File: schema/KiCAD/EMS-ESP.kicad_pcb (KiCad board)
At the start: 2 copper layers, 76.5 x 47.2 mm, 47 parts, among them IC1 LM393N, J1 EMS-Bus, J2 DS18B20, J3 I2C, J4 I2C-BMP180, T1 BC847B, U1 DC-Buck_Converter_Chin01, U2 NodeMCU_1.0_(ESP-12E)

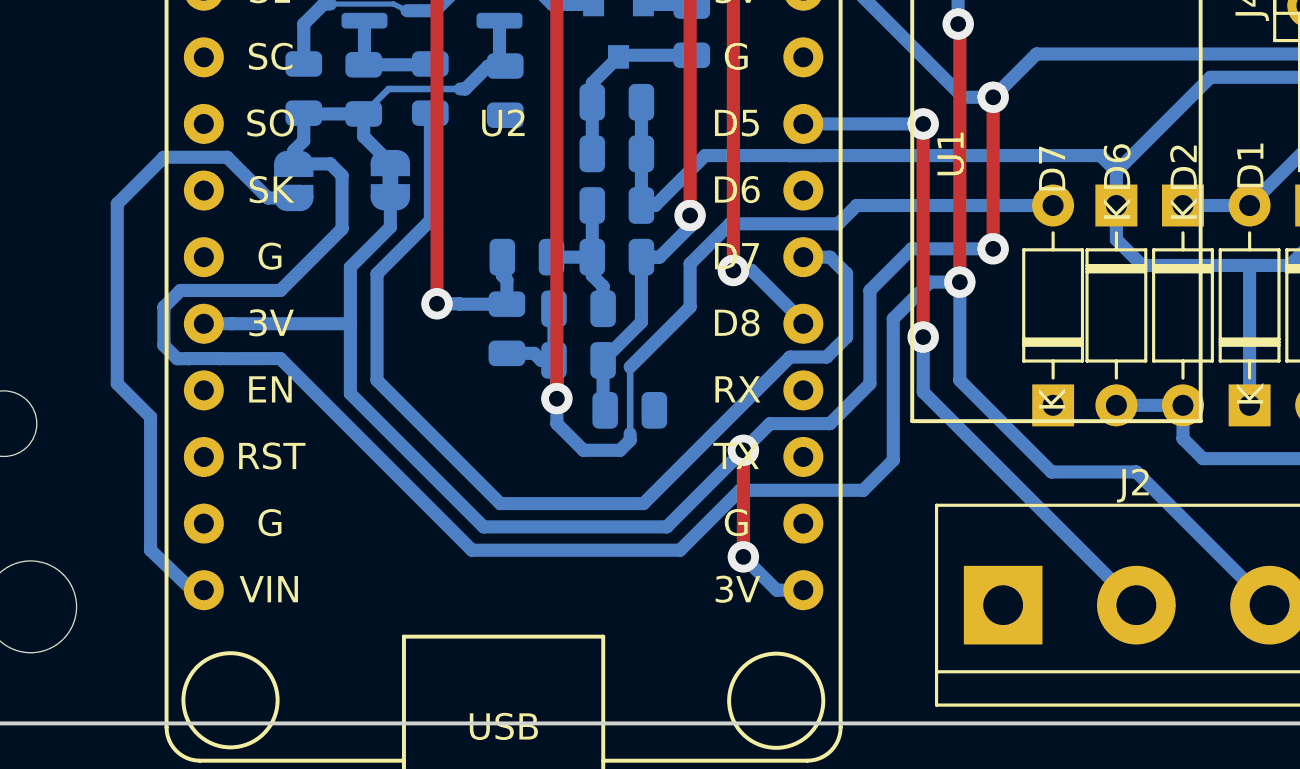
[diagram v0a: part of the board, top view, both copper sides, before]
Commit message: added pullup resistor for DS18B20 data line
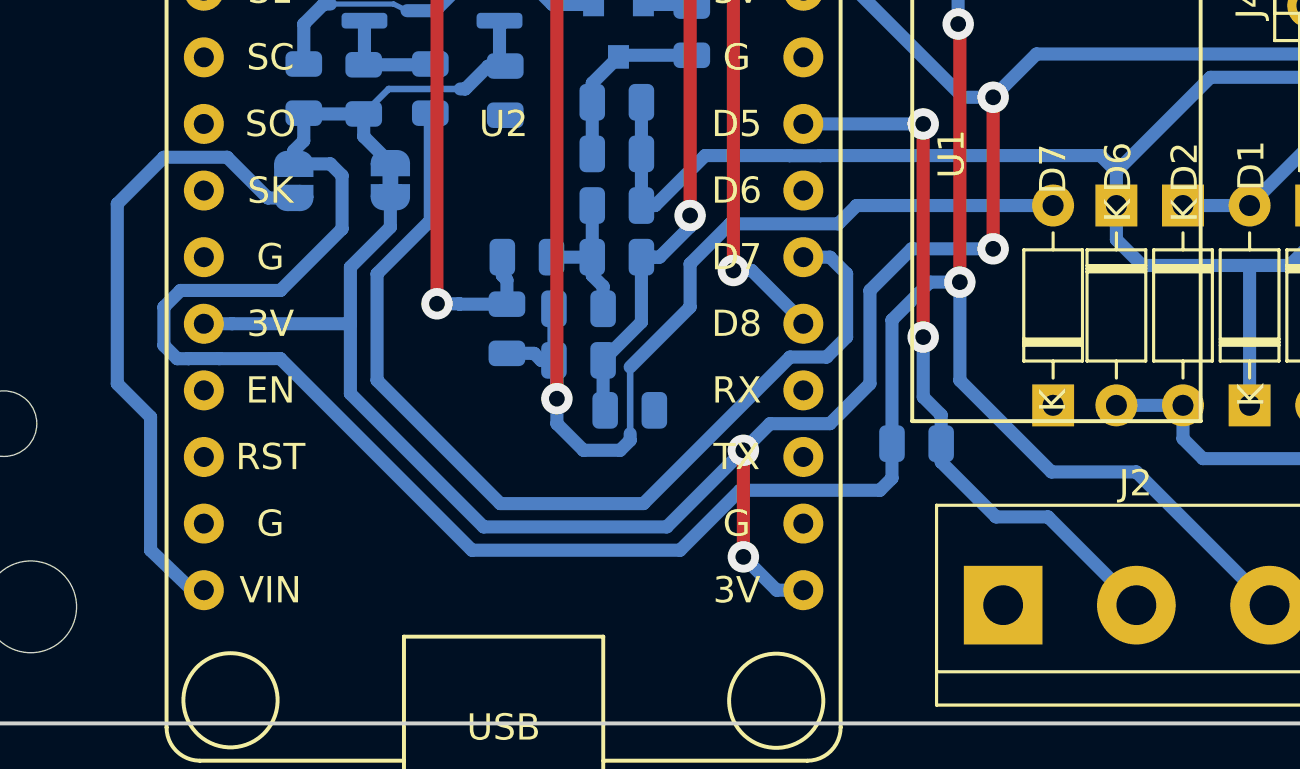
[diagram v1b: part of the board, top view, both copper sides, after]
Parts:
- added R12: 4k7, Resistor_SMD:R_0805_2012Metric, B.Cu at (168.4, 112.0)
- R3: value 360R -> 360
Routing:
- net /DS: track 26.2 -> 27.4 mm
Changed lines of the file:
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@@
     (thickness 1.6)
     (drawings 9)
-    (tracks 292)
+    (tracks 297)
     (zones 0)
-    (modules 47)
+    (modules 48)
     (nets 42)
   )
   (page A4)
   (layers
-    (0 F.Cu signal hide)
+    (0 F.Cu signal)
     (31 B.Cu signal)
     (32 B.Adhes user hide)
@@
     (visible_elements 7FFFFFFF)
     (pcbplotparams
-      (layerselection 0x00020_7ffffffe)
+      (layerselection 0x00010_7ffffffe)
       (usegerberextensions false)
       (usegerberattributes false)
@@
       (subtractmaskfromsilk false)
       (outputformat 4)
-      (mirror false)
+      (mirror true)
       (drillshape 1)
       (scaleselection 1)
@@
       (effects (font (size 1 1) (thickness 0.15)) (justify mirror))
     )
-    (fp_text value 360R (at 0 -1.65) (layer B.Fab)
+    (fp_text value 360 (at 0 -1.65) (layer B.Fab)
       (effects (font (size 1 1) (thickness 0.15)) (justify mirror))
     )
@@
       (net 41 "Net-(U2-Pad30)"))
   )
+  (module Resistor_SMD:R_0805_2012Metric (layer B.Cu)
+    (at 168.402 112.014)
+    (descr "Resistor SMD 0805 (2012 Metric), square (rectangular) end terminal, IPC_7351 nominal, (Body size source: https://docs.google.com/spreadsheets/d/1BsfQQcO9C6DZCsRaXUlFlo91Tg2WpOkGARC1WS5S8t0/edit?usp=sharing), generated with kicad-footprint-generator")
+    (tags resistor)
+    (attr smd)
+    (fp_text reference R12 (at 0 1.65) (layer B.SilkS)
+      (effects (font (size 1 1) (thickness 0.15)) (justify mirror))
+    )
+    (fp_text value 4k7 (at 0 -1.65) (layer B.Fab)
+      (effects (font (size 1 1) (thickness 0.15)) (justify mirror))
+    )
+    (fp_line (start -1 -0.6) (end -1 0.6) (layer B.Fab) (width 0.1))
+    (fp_line (start -1 0.6) (end 1 0.6) (layer B.Fab) (width 0.1))
+    (fp_line (start 1 0.6) (end 1 -0.6) (layer B.Fab) (width 0.1))
+    (fp_line (start 1 -0.6) (end -1 -0.6) (layer B.Fab) (width 0.1))
+    (fp_line (start -0.258578 0.71) (end 0.258578 0.71) (layer B.SilkS) (width 0.12))
+    (fp_line (start -0.258578 -0.71) (end 0.258578 -0.71) (layer B.SilkS) (width 0.12))
+    (fp_line (start -1.68 -0.95) (end -1.68 0.95) (layer B.CrtYd) (width 0.05))
+    (fp_line (start -1.68 0.95) (end 1.68 0.95) (layer B.CrtYd) (width 0.05))
+    (fp_line (start 1.68 0.95) (end 1.68 -0.95) (layer B.CrtYd) (width 0.05))
+    (fp_line (start 1.68 -0.95) (end -1.68 -0.95) (layer B.CrtYd) (width 0.05))
+    (fp_text user %R (at 0 0) (layer B.Fab)
+      (effects (font (size 0.5 0.5) (thickness 0.08)) (justify mirror))
+    )
+    (pad 1 smd roundrect (at -0.9375 0) (size 0.975 1.4) (layers B.Cu B.Paste B.Mask) (roundrect_rratio 0.25)
+      (net 14 +3V3))
+    (pad 2 smd roundrect (at 0.9375 0) (size 0.975 1.4) (layers B.Cu B.Paste B.Mask) (roundrect_rratio 0.25)
+      (net 19 /DS))
+    (model ${KISYS3DMOD}/Resistor_SMD.3dshapes/R_0805_2012Metric.wrl
+      (at (xyz 0 0 0))
+      (scale (xyz 1 1 1))
+      (rotate (xyz 0 0 0))
+    )
+  )
   (gr_line (start 206.502 75.438) (end 206.502 122.682) (layer Edge.Cuts) (width 0.15))
   (gr_line (start 130.048 75.438) (end 206.502 75.438) (layer Edge.Cuts) (width 0.15))
@@
   (segment (start 148.2725 98.4885) (end 147.32 99.441) (width 0.25) (layer B.Cu) (net 14) (status 20))
   (segment (start 151.1935 98.4885) (end 148.2725 98.4885) (width 0.25) (layer B.Cu) (net 14))
-  (segment (start 166.37 113.792) (end 167.513 112.649) (width 0.5) (layer B.Cu) (net 14))
-  (segment (start 161.671 113.792) (end 166.37 113.792) (width 0.5) (layer B.Cu) (net 14))
-  (segment (start 159.385 116.078) (end 161.671 113.792) (width 0.5) (layer B.Cu) (net 14))
-  (segment (start 141.805761 108.769999) (end 141.808691 108.772929) (width 0.5) (layer B.Cu) (net 14))
-  (segment (start 167.513 112.649) (end 167.513 107.2515) (width 0.5) (layer B.Cu) (net 14))
-  (segment (start 146.4945 103.8225) (end 144.145 106.172) (width 0.5) (layer B.Cu) (net 14))
-  (segment (start 168.91 105.8545) (end 170.052996 105.8545) (width 0.5) (layer B.Cu) (net 14))
-  (segment (start 144.653 101.346) (end 146.05 101.346) (width 0.5) (layer B.Cu) (net 14) (status 10))
-  (segment (start 144.145 106.172) (end 140.335 106.172) (width 0.5) (layer B.Cu) (net 14))
-  (segment (start 141.808691 108.772929) (end 144.139499 108.769999) (width 0.5) (layer B.Cu) (net 14))
-  (segment (start 139.7 106.807) (end 139.7 108.2675) (width 0.5) (layer B.Cu) (net 14))
-  (segment (start 146.4945 101.7905) (end 146.4945 103.8225) (width 0.5) (layer B.Cu) (net 14))
-  (segment (start 151.4475 116.078) (end 159.385 116.078) (width 0.5) (layer B.Cu) (net 14))
-  (segment (start 146.05 101.346) (end 146.4945 101.7905) (width 0.5) (layer B.Cu) (net 14))
-  (segment (start 167.513 107.2515) (end 168.91 105.8545) (width 0.5) (layer B.Cu) (net 14))
-  (segment (start 140.636738 108.7755) (end 140.642239 108.769999) (width 0.5) (layer B.Cu) (net 14))
-  (segment (start 144.139499 108.769999) (end 151.4475 116.078) (width 0.5) (layer B.Cu) (net 14))
-  (segment (start 140.335 106.172) (end 139.7 106.807) (width 0.5) (layer B.Cu) (net 14))
-  (segment (start 139.7 108.2675) (end 140.208 108.7755) (width 0.5) (layer B.Cu) (net 14))
-  (segment (start 140.208 108.7755) (end 140.636738 108.7755) (width 0.5) (layer B.Cu) (net 14))
-  (segment (start 140.642239 108.769999) (end 141.805761 108.769999) (width 0.5) (layer B.Cu) (net 14))
   (segment (start 147.32 100.3) (end 148.336 101.316) (width 0.5) (layer B.Cu) (net 14) (status 20))
   (segment (start 147.32 99.441) (end 147.32 100.3) (width 0.5) (layer B.Cu) (net 14) (status 10))
+  (segment (start 167.4645 107.3) (end 167.4645 112.014) (width 0.5) (layer B.Cu) (net 14))
+  (segment (start 170.052996 105.8545) (end 168.91 105.8545) (width 0.5) (layer B.Cu) (net 14))
+  (segment (start 168.91 105.8545) (end 167.4645 107.3) (width 0.5) (layer B.Cu) (net 14))
+  (segment (start 146.4945 101.7905) (end 146.05 101.346) (width 0.5) (layer B.Cu) (net 14))
+  (segment (start 146.4945 103.8225) (end 146.4945 101.7905) (width 0.5) (layer B.Cu) (net 14))
+  (segment (start 144.145 106.172) (end 146.4945 103.8225) (width 0.5) (layer B.Cu) (net 14))
+  (segment (start 139.7 106.807) (end 140.335 106.172) (width 0.5) (layer B.Cu) (net 14))
+  (segment (start 139.7 108.2675) (end 139.7 106.807) (width 0.5) (layer B.Cu) (net 14))
+  (segment (start 140.208 108.7755) (end 139.7 108.2675) (width 0.5) (layer B.Cu) (net 14))
+  (segment (start 161.671 113.792) (end 159.385 116.078) (width 0.5) (layer B.Cu) (net 14))
+  (segment (start 140.636738 108.7755) (end 140.208 108.7755) (width 0.5) (layer B.Cu) (net 14))
+  (segment (start 167.005 113.792) (end 161.671 113.792) (width 0.5) (layer B.Cu) (net 14))
+  (segment (start 146.05 101.346) (end 144.653 101.346) (width 0.5) (layer B.Cu) (net 14))
+  (segment (start 159.385 116.078) (end 151.4475 116.078) (width 0.5) (layer B.Cu) (net 14))
+  (segment (start 140.335 106.172) (end 144.145 106.172) (width 0.5) (layer B.Cu) (net 14))
+  (segment (start 167.4645 112.014) (end 167.4645 113.3325) (width 0.5) (layer B.Cu) (net 14))
+  (segment (start 144.139499 108.769999) (end 141.808691 108.772929) (width 0.5) (layer B.Cu) (net 14))
+  (segment (start 167.4645 113.3325) (end 167.005 113.792) (width 0.5) (layer B.Cu) (net 14))
+  (segment (start 151.4475 116.078) (end 144.139499 108.769999) (width 0.5) (layer B.Cu) (net 14))
+  (segment (start 141.808691 108.772929) (end 141.805761 108.769999) (width 0.5) (layer B.Cu) (net 14))
+  (segment (start 141.805761 108.769999) (end 140.642239 108.769999) (width 0.5) (layer B.Cu) (net 14))
+  (segment (start 140.642239 108.769999) (end 140.636738 108.7755) (width 0.5) (layer B.Cu) (net 14))
   (segment (start 181.102 110.5535) (end 181.102 105.2195) (width 0.5) (layer B.Cu) (net 15) (status 10))
   (segment (start 183.642 104.2035) (end 183.642 102.9335) (width 0.5) (layer B.Cu) (net 15) (status 20))
@@
   (segment (start 193.167 110.5535) (end 193.167 112.7125) (width 0.5) (layer B.Cu) (net 18) (status 10))
   (segment (start 193.167 112.7125) (end 192.532 113.3475) (width 0.5) (layer B.Cu) (net 18))
-  (segment (start 168.655998 108.374264) (end 168.655998 107.95) (width 0.5) (layer B.Cu) (net 19))
-  (segment (start 176.784 118.1735) (end 168.655998 110.045498) (width 0.5) (layer B.Cu) (net 19) (status 10))
   (via (at 168.655998 107.95) (size 1.2) (drill 0.6) (layers F.Cu B.Cu) (net 19))
-  (segment (start 168.655998 110.045498) (end 168.655998 108.374264) (width 0.5) (layer B.Cu) (net 19))
   (segment (start 168.655998 99.822002) (end 168.656 99.822) (width 0.5) (layer F.Cu) (net 19))
   (segment (start 168.655998 107.95) (end 168.655998 99.822002) (width 0.5) (layer F.Cu) (net 19))
   (segment (start 164.1475 99.822) (end 168.656 99.822) (width 0.5) (layer B.Cu) (net 19) (status 10))
   (via (at 168.656 99.822) (size 1.2) (drill 0.6) (layers F.Cu B.Cu) (net 19))
+  (segment (start 169.3395 110.9195) (end 169.3395 112.014) (width 0.5) (layer B.Cu) (net 19))
+  (segment (start 168.655998 107.95) (end 168.655998 110.235998) (width 0.5) (layer B.Cu) (net 19))
+  (segment (start 168.655998 110.235998) (end 169.3395 110.9195) (width 0.5) (layer B.Cu) (net 19))
+  (segment (start 169.3395 112.714) (end 171.4335 114.808) (width 0.5) (layer B.Cu) (net 19))
+  (segment (start 169.3395 112.014) (end 169.3395 112.714) (width 0.5) (layer B.Cu) (net 19))
+  (segment (start 173.4185 114.808) (end 176.784 118.1735) (width 0.5) (layer B.Cu) (net 19))
+  (segment (start 171.4335 114.808) (end 173.4185 114.808) (width 0.5) (layer B.Cu) (net 19))
   (segment (start 183.388 91.5035) (end 183.388 95.3135) (width 0.5) (layer B.Cu) (net 20) (status 30))
   (segment (start 181.4195 89.535) (end 183.388 91.5035) (width 0.5) (layer B.Cu) (net 20) (status 20))

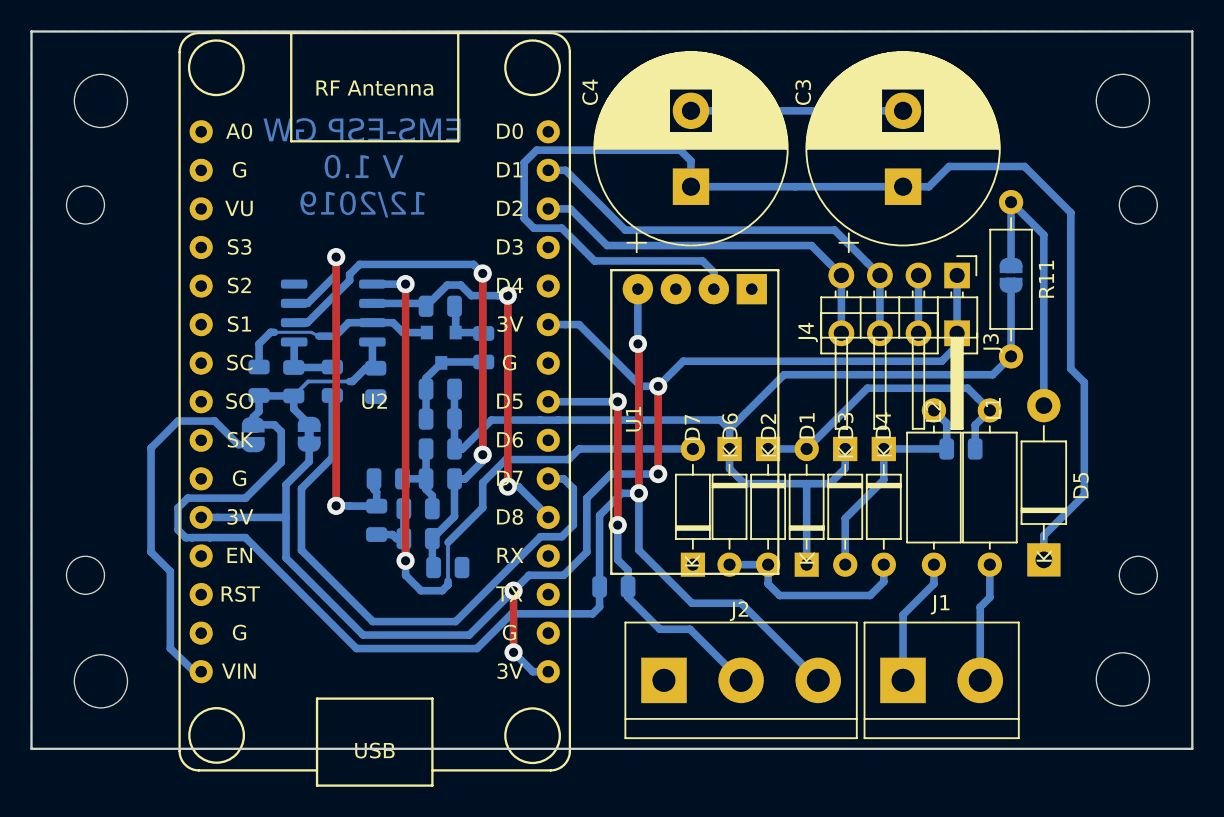
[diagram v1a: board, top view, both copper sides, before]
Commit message: rearranged bucket converter, pinheader corrected
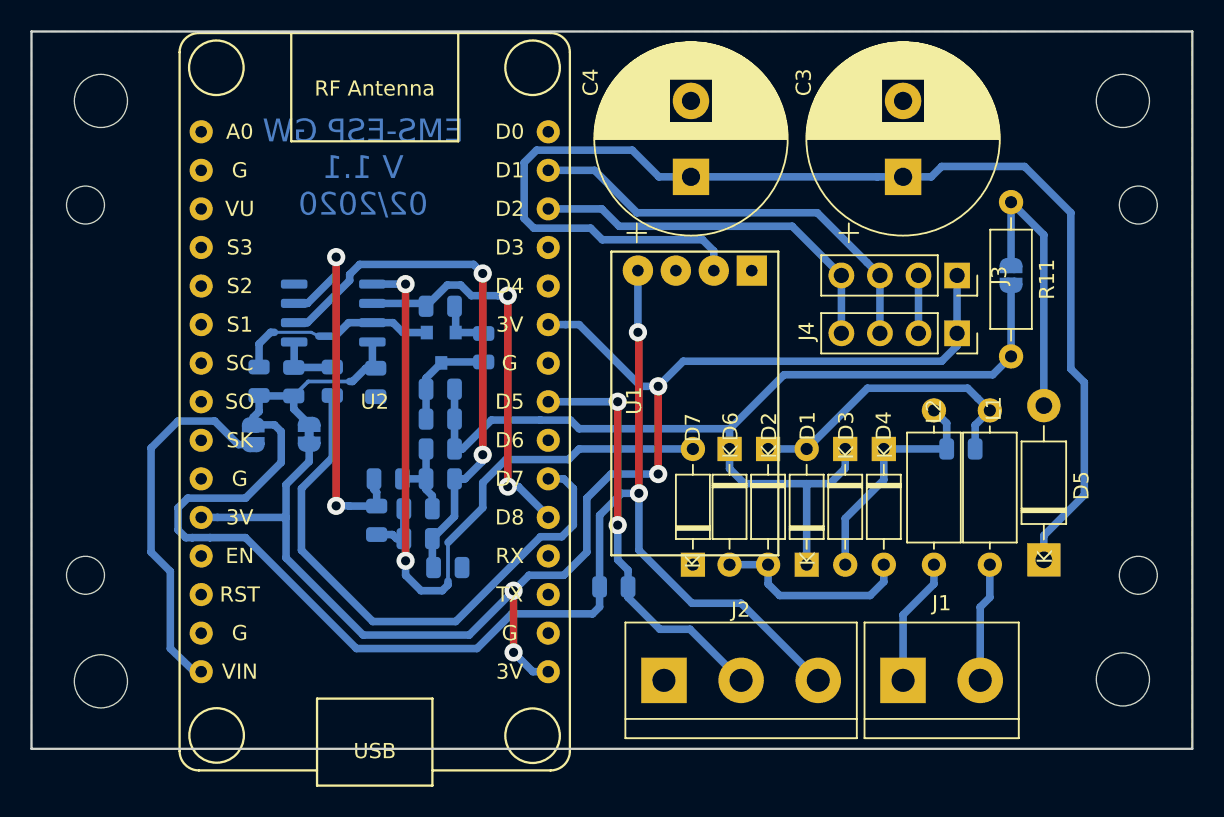
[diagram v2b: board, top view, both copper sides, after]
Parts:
- J3: footprint Connector_PinHeader_2.54mm:PinHeader_1x04_P2.54mm_Horizontal -> Connector_PinSocket_2.54mm:PinSocket_1x04_P2.54mm_Vertical
- moved U1 1.22 mm to (173.7, 99.9)
- moved C3 0.65 mm to (187.5, 85.0)
- moved C4 0.65 mm to (173.5, 85.0)
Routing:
- net GND: track 34.7 -> 20.8 mm
- net Net-(C3-Pad1): track 83.2 -> 81.3 mm
- net +3V3: track 102.7 -> 103.9 mm
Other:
- board text added: "EMS-ESP GW V 1.1 02/2020"
- board text removed: "EMS-ESP GW V 1.0 12/2019"
